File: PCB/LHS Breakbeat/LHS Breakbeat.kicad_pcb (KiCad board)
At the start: 2 copper layers, 114 x 61.4 mm, 47 parts, among them J1 Steppers In, J10 RGB, J11 Filament Sensor / Tach, J12 Endstop X, J13 Endstop Y, J14 Fan Aux, J15 Fan Part, J16 Fan Hotend/Can HL, J17 Motor X, J19 Motor X1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

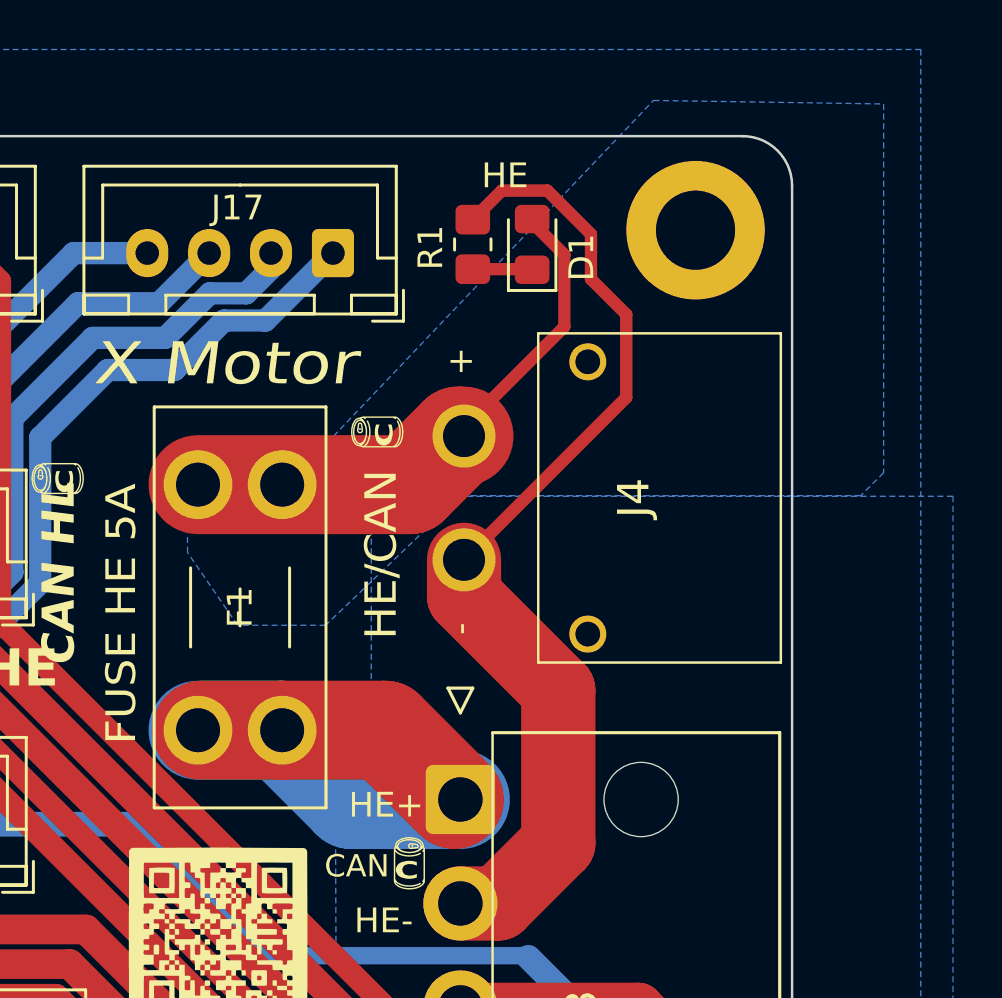
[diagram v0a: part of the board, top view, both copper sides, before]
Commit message: Adding LHS Breakbeat Wiring Harness specifications
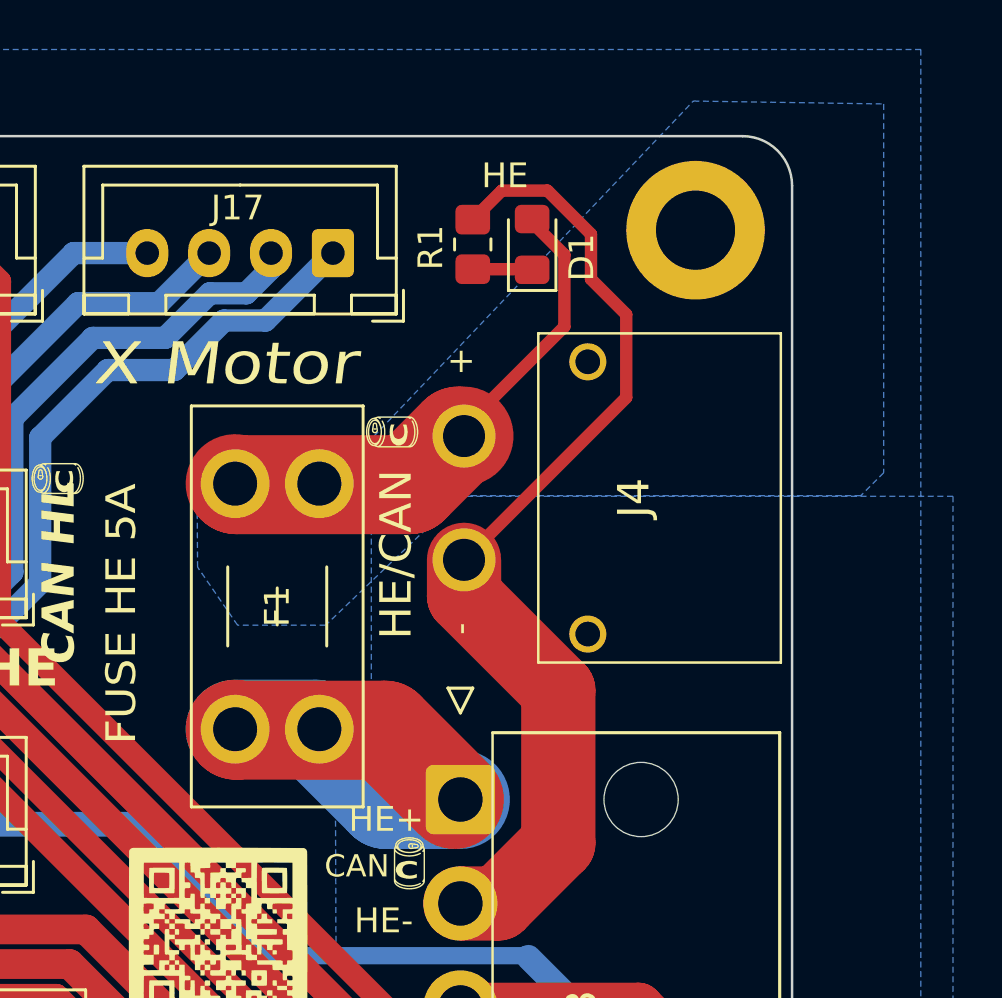
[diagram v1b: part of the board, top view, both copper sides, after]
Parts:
- moved F1 1.50 mm to (178.5, 90.0)
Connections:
- J4 pad 3: unconnected-(J4-Pin_3-Pad3) -> (no net)
- J4 pad 4: unconnected-(J4-Pin_4-Pad4) -> (no net)
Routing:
- net /HE+/CAN_V: track 23.1 -> 20.3 mm
- net /Fused HE: track 22.5 -> 21.1 mm
